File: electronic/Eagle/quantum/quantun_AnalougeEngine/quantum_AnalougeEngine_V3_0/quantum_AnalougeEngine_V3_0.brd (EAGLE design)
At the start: 171.7 x 107.6 mm, 174 parts, among them IC1 OP275, IC2 NE5532D, IC3 NE5532D, IC4 OP275, IC5 NE5532D, IC6 NE5532D, IC8 OP275, IC9 TL072, K5 RELAY_EE2-5NU, K6 RELAY_EE2-5NU, K7 RELAY_EE2-5NU, K8 RELAY_EE2-5NU, U1 NUCLEO-F429ZI, U12 ULN2003, U4 THAT1240, U6 THAT1240, U7 THAT1240, U8 THAT1240

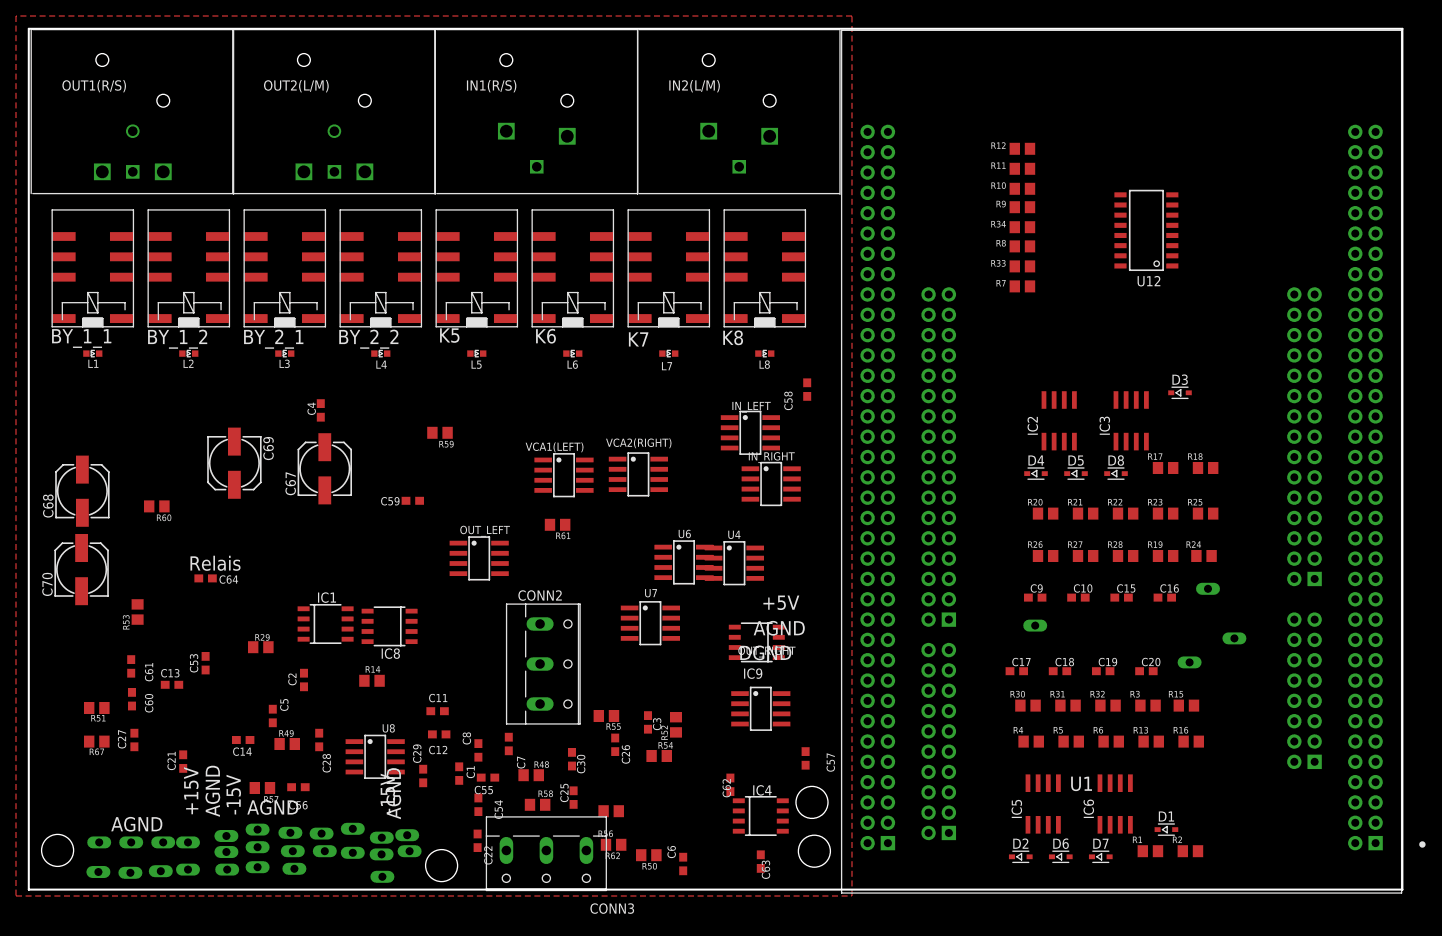
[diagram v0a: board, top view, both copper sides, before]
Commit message: Implemented Relais GPIOs, EAGLE Layout progress positioning (total layout job 30 %)
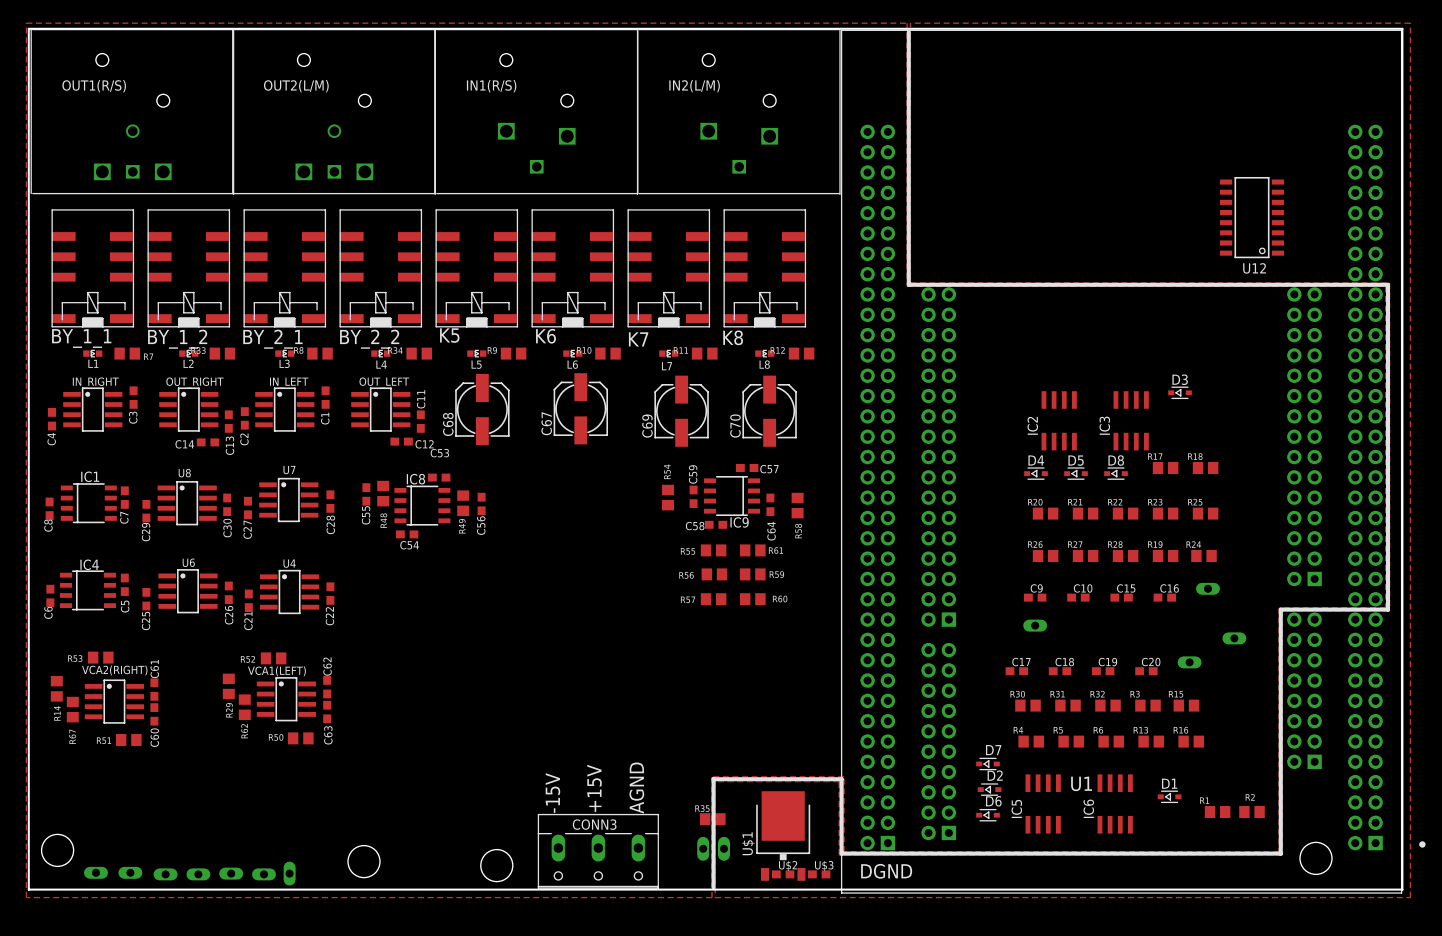
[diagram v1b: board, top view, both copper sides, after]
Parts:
- removed CONN2: (no value), C_Sager_Bibliothek:W237-103
- removed DGND1, DGND2, DGND3, DGND4, TP07, TP08, TP10, TP11, TP12, TP14, TP15, TP19, TP20, TP21, TP22, TP24, TP25, TP26: TPTHT, C_Sager_Bibliothek:THT_PIN
- added R35: 0R, C_Sager_Bibliothek:R0805
- added TP05: TPTHT, C_Sager_Bibliothek:THT_PIN
- added U$1: 78*, C_Sager_Bibliothek:TO252
- added U$2, U$3: (no value), C_Sager_Bibliothek:C0603
- moved R7 112.2 mm to (12.3, 67.0), turned to 0 degrees
- moved R33 100.6 mm to (24.2, 67.0)
- moved R8 88.8 mm to (36.4, 67.0)
- moved IC4 88.7 mm to (7.40, 37.4)
- moved C70 88.2 mm to (92.6, 59.8)
- moved C6 85.9 mm to (2.70, 36.7)
- moved IN_RIGHT 85.3 mm to (8.00, 60.0)
- moved OUT_RIGHT 80.7 mm to (20.0, 60.0)
- moved R34 77.0 mm to (48.8, 67.0)
- moved C3 76.0 mm to (13.1, 61.5), turned to 90 degrees
- moved R60 75.4 mm to (90.5, 36.3), turned to 0 degrees
- moved VCA2(RIGHT) 71.4 mm to (10.7, 23.5)
- moved C64 71.2 mm to (92.7, 48.1), turned to 270 degrees
- moved TP18 67.9 mm to (84.3, 5.10), turned to 90 degrees
- moved R9 66.2 mm to (60.6, 67.0)
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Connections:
- net DAC1_OUT(A) renamed DAC_OUT1
- net DAC2_OUT(A) renamed DAC_OUT2
- removed net +9V: CONN2.2
- removed net MAIN_µC_D2: U12.1
- removed net MAIN_µC_D3: U12.2
- removed net MAIN_µC_D4: U12.3
- removed net MAIN_µC_D5: U12.4
- removed net MAIN_µC_D6: U12.5
- removed net MAIN_µC_D7: U12.6
- new net ADC1-IN3: U1.CN12_37
- new net ADC1-IN6: U1.CN12_13
- new net ADC1_IN0: U1.CN11_28
- new net ADC2-IN10: U1.CN11_38
- new net ADC2-IN12: U1.CN11_35
- new net ADC2-IN9: U1.CN12_24
- new net ADC3-IN13: U1.CN11_37
- new net ADC3-IN14: U1.CN12_38
- new net ADC3-IN15: U1.CN12_36
- new net RELAIS1: U1.CN11_58, U12.1
- new net RELAIS2: U1.CN11_62, U12.2
- new net RELAIS3: U1.CN11_64, U12.3
- new net RELAIS4: U1.CN11_66, U12.4
- new net RELAIS5: U1.CN11_65, U12.5
- new net RELAIS6: U1.CN11_63, U12.6
- new net USART6_RX: U1.CN12_4
- new net USRAT6_TX: U1.CN12_19
- net +5V: now also U$1.3, U$3.1, U1.CN8_15; no longer CONN2.1, TP07.P$1, TP11.P$1, TP12.P$1, U1.CN11_18, U1.CN8_9
- net AGND: now also CONN3.1, R35.1; no longer CONN3.2, TP08.P$1, TP14.P$1, TP15.P$1, TP19.P$1, TP20.P$1, TP21.P$1, TP22.P$1
- net DGND: now also R35.2, TP05.P$1, U$1.2, U$2.2, U$3.2, U1.CN8_11, U1.CN8_13; no longer CONN2.3, DGND1.P$1, DGND2.P$1, DGND3.P$1, DGND4.P$1
- net L/M_OUT+: now also BY_2_2.S1; no longer BY_2_1.S1
- net L/M_OUT-: now also BY_2_2.S2; no longer BY_2_1.S2
- net N$13: now also BY_2_1.S1; no longer BY_2_2.S1
- net N$15: now also BY_2_2.P1; no longer BY_2_1.P1
- net N$17: now also BY_2_2.P2; no longer BY_2_1.P2
- net N$25: now also BY_2_1.P1; no longer BY_2_2.P1
- net N$27: now also BY_2_1.P2; no longer BY_2_2.P2
- net N$7: now also BY_2_1.S2; no longer BY_2_2.S2
- net V+: now also CONN3.2, U$1.1, U$2.1; no longer CONN3.1, TP24.P$1, TP26.P$1
- net V-: no longer TP10.P$1, TP25.P$1
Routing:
- added copper zone on layer 1, net DGND
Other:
- board text removed: "+5V"
- board text removed: "Relais"
